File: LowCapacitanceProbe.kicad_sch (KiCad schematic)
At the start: 41 parts, among them J1 u.Fl, J2 SMA, J3 Screw_Terminal_01x01, Q1 BF998, U2 SPX3819M5-L-5-0

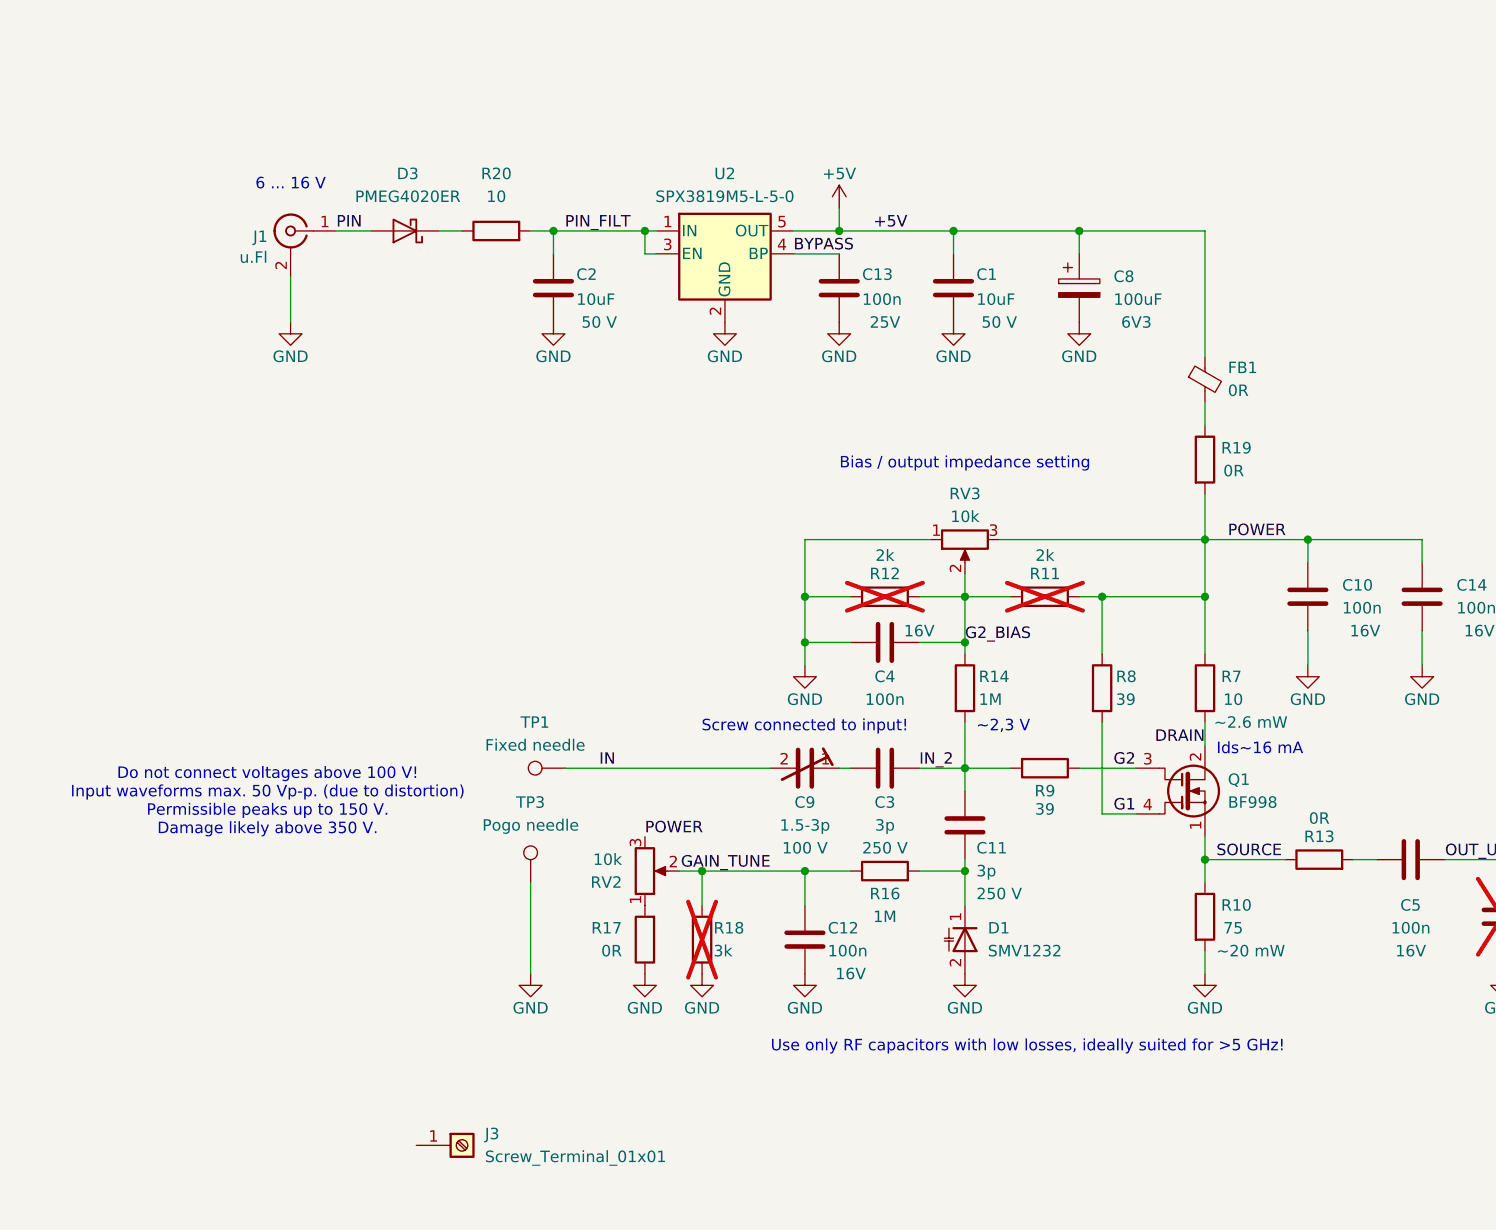
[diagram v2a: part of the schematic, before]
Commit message: Added mounting point for PCBite holder (M4 nut).
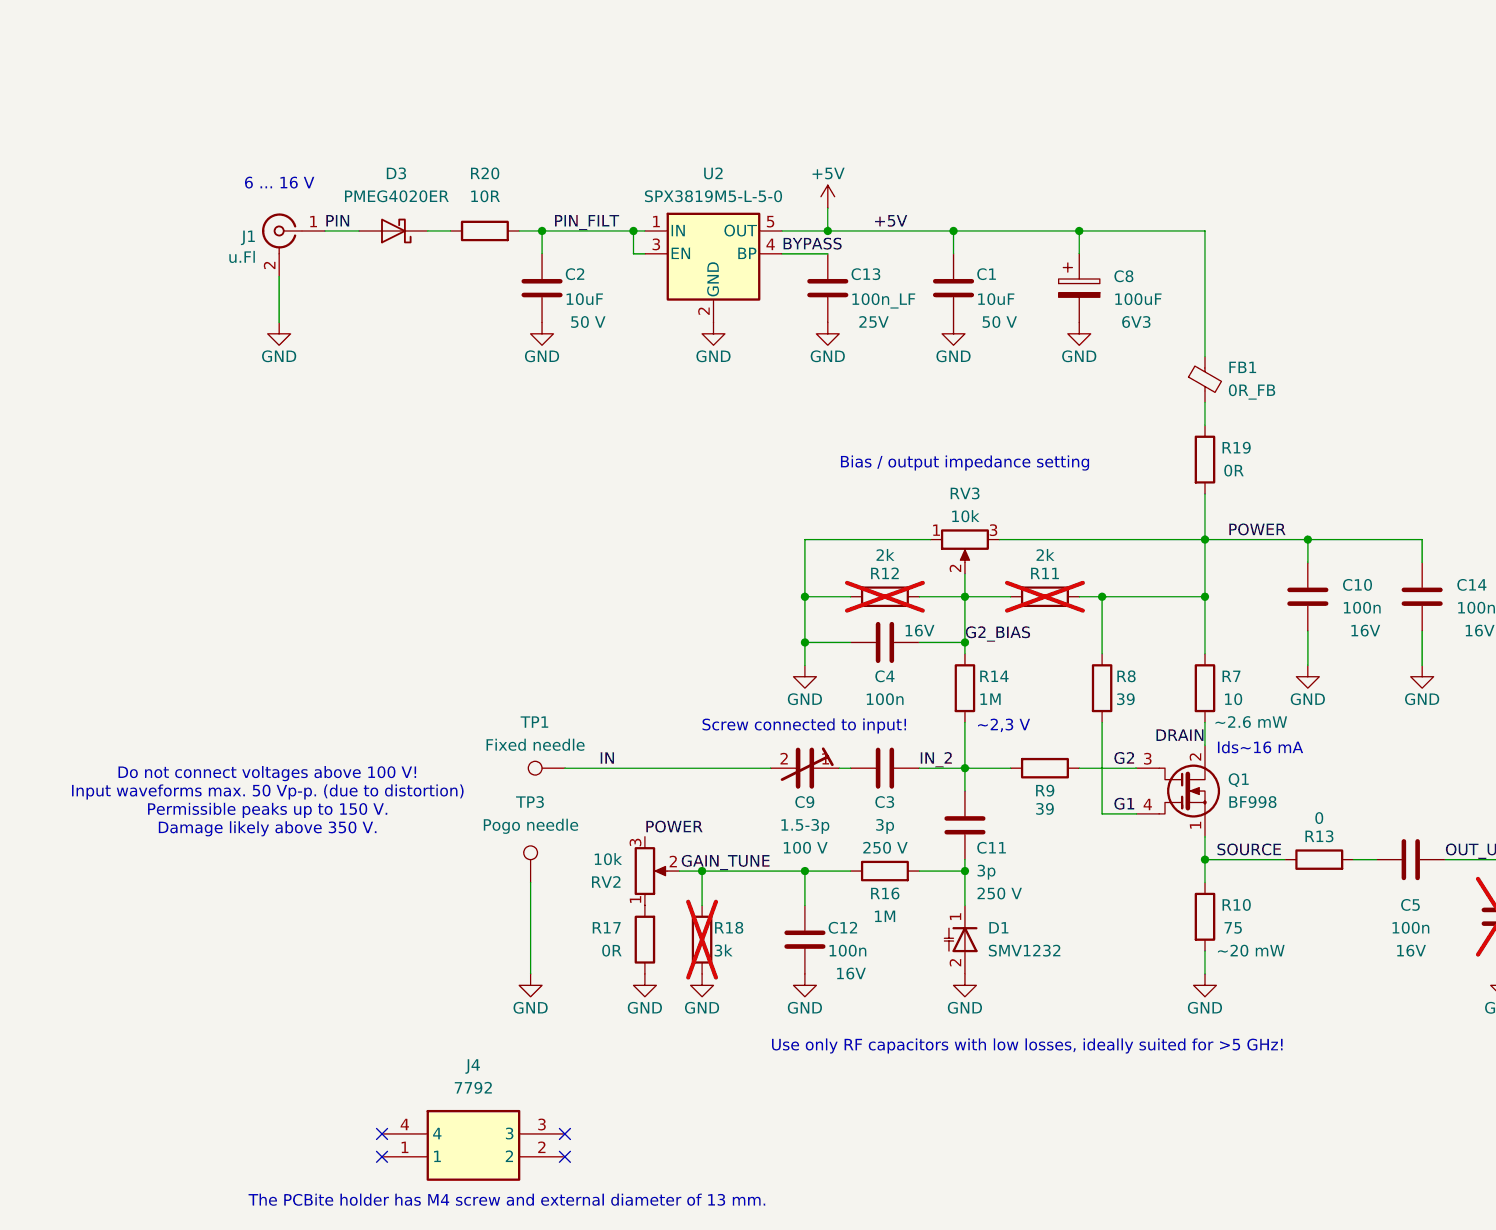
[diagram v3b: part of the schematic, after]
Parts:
- removed J3: Screw_Terminal_01x01, symbol Connector:Screw_Terminal_01x01
- added J4: 7792, 7792:7792, symbol 7792:7792
- C13: value 100n -> 100n_LF
- FB1: value 0R -> 0R_FB
- R13: value 0R -> 0
- R20: value 10 -> 10R
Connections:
- no-connect marks 0 -> 4
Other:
- note added: "The PCBite holder has M4 screw and external diameter of 13 mm."
- moved on the sheet: C13, C2, D3, J1, R20, U2

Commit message: Continued routing, modifications for better usability.
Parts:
- J4: MPN (none) -> 7792; Mouser (none) -> 534-7792
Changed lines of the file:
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@@
+			)
+		)
+		(property "MPN" "7792"
+			(at 73.66 158.75 0)
+			(effects
+				(font
+					(size 1.27 1.27)
+				)
+				(hide yes)
+			)
+		)
+		(property "Mouser" "534-7792"
+			(at 73.66 158.75 0)
+			(effects
+				(font
+					(size 1.27 1.27)
+				)
+				(hide yes)
 			)
 		)

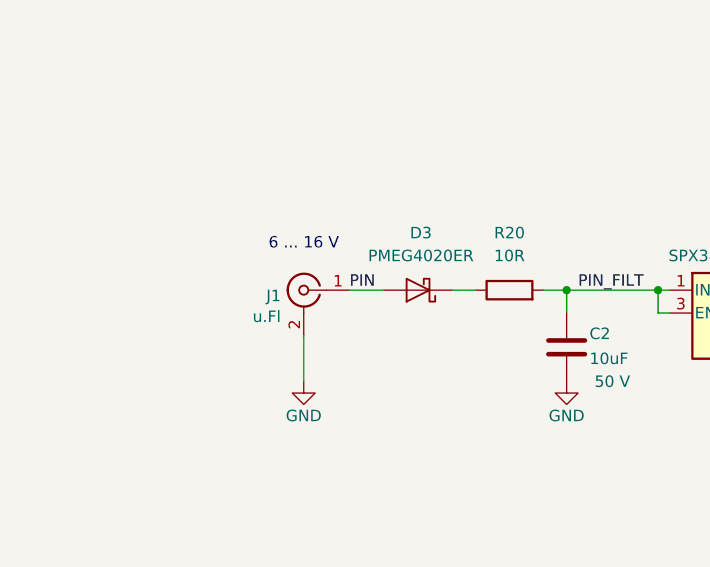
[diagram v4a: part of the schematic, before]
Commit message: Continued routing, replaced power connector.
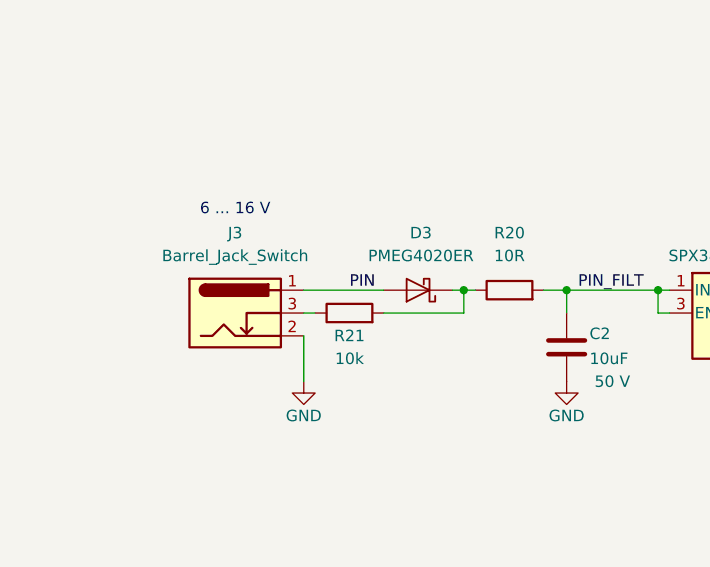
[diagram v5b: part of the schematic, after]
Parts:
- removed J1: u.Fl, Connector_Coaxial:U.FL_Molex_MCRF_73412-0110_Vertical, symbol Connector:Conn_Coaxial
- added J3: Barrel_Jack_Switch, Connector_BarrelJack:BarrelJack_Wuerth_694103107102_1.35x3.9mm, symbol Connector:Barrel_Jack_Switch
- added R21: 10k, Resistor_SMD:R_0603_1608Metric_Pad0.98x0.95mm_HandSolder, symbol Device:R
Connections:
- net GND: now also J3.2
- net PIN: now also J3.1
- net at D3.1 (K), R20.1: now also R21.2
- new net: J3.3, R21.1
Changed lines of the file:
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@@
 	(text "6 ... 16 V"
 		(exclude_from_sim no)
-		(at 62.23 53.34 0)
+		(at 54.61 49.53 0)
 		(effects
 			(font
@@
 	)
 	(junction
+		(at 80.01 58.42)
+		(diameter 0)
+		(color 0 0 0 0)
+	)
+	(junction
 		(at 120.65 99.06)
 		(diameter 0)
@@
 	(wire
 		(pts
-			(xy 78.74 58.42) (xy 81.28 58.42)
+			(xy 78.74 58.42) (xy 80.01 58.42)
 		)
 		(stroke
@@
 	(wire
 		(pts
+			(xy 62.23 60.96) (xy 63.5 60.96)
+		)
+		(stroke
+			(width 0)
+			(type default)
+		)
+	)
+	(wire
+		(pts
 			(xy 165.1 87.63) (xy 165.1 92.71)
 		)
@@
 	(wire
 		(pts
+			(xy 62.23 58.42) (xy 71.12 58.42)
+		)
+		(stroke
+			(width 0)
+			(type default)
+		)
+	)
+	(wire
+		(pts
 			(xy 120.65 92.71) (xy 120.65 99.06)
 		)
@@
 	(wire
 		(pts
+			(xy 80.01 60.96) (xy 80.01 58.42)
+		)
+		(stroke
+			(width 0)
+			(type default)
+		)
+	)
+	(wire
+		(pts
 			(xy 138.43 99.06) (xy 138.43 104.14)
 		)
@@
 	(wire
 		(pts
-			(xy 67.31 58.42) (xy 71.12 58.42)
-		)
-		(stroke
-			(width 0)
-			(type default)
-		)
-	)
-	(wire
-		(pts
 			(xy 101.6 58.42) (xy 102.87 58.42)
 		)
@@
 	(wire
 		(pts
+			(xy 80.01 58.42) (xy 81.28 58.42)
+		)
+		(stroke
+			(width 0)
+			(type default)
+		)
+	)
+	(wire
+		(pts
 			(xy 138.43 128.27) (xy 138.43 129.54)
 		)
@@
 		(pts
 			(xy 133.35 104.14) (xy 138.43 104.14)
+		)
+		(stroke
+			(width 0)
+			(type default)
+		)
+	)
+	(wire
+		(pts
+			(xy 71.12 60.96) (xy 80.01 60.96)
 		)
 		(stroke
@@
 				(path "/e63e39d7-6ac0-4ffd-8aa3-1841a4541b55"
 					(reference "R18")
+					(unit 1)
+				)
+			)
+		)
+	)
+	(symbol
+		(lib_id "Device:R")
+		(at 67.31 60.96 90)
+		(unit 1)
+		(exclude_from_sim no)
+		(in_bom yes)
+		(on_board yes)
+		(dnp no)
+		(property "Reference" "R21"
+			(at 67.31 63.5 90)
+			(effects
+				(font
+					(size 1.27 1.27)
+				)
+			)
+		)
+		(property "Value" "10k"
+			(at 67.31 66.04 90)
+			(effects
+				(font
+					(size 1.27 1.27)
+				)
+			)
+		)
+		(property "Footprint" "Resistor_SMD:R_0603_1608Metric_Pad0.98x0.95mm_HandSolder"
+			(at 67.31 62.738 90)
+			(effects
+				(font
+					(size 1.27 1.27)
+				)
+				(hide yes)
+			)
+		)
+		(property "Datasheet" "~"
+			(at 67.31 60.96 0)
+			(effects
+				(font
+					(size 1.27 1.27)
+				)
+				(hide yes)
+			)
+		)
+		(property "Description" "Resistor"
+			(at 67.31 60.96 0)
+			(effects
+				(font
+					(size 1.27 1.27)
+				)
+				(hide yes)
+			)
+		)
+		(pin "2"
+		)
+		(pin "1"
+		)
+		(instances
+			(project "LowCapacitanceProbe"
+				(path "/e63e39d7-6ac0-4ffd-8aa3-1841a4541b55"
+					(reference "R21")
+					(unit 1)
+				)
+			)
+		)
+	)
+	(symbol
+		(lib_id "Connector:Barrel_Jack_Switch")
+		(at 54.61 60.96 0)
+		(unit 1)
+		(exclude_from_sim no)
+		(in_bom yes)
+		(on_board yes)
+		(dnp no)
+		(fields_autoplaced yes)
+		(property "Reference" "J3"
+			(at 54.61 52.07 0)
+			(effects
+				(font
+					(size 1.27 1.27)
+				)
+			)
+		)
+		(property "Value" "Barrel_Jack_Switch"
+			(at 54.61 54.61 0)
+			(effects
+				(font
+					(size 1.27 1.27)
+				)
+			)
+		)
+		(property "Footprint" "Connector_BarrelJack:BarrelJack_Wuerth_694103107102_1.35x3.9mm"
+			(at 55.88 61.976 0)
+			(effects
+				(font
+					(size 1.27 1.27)
+				)
+				(hide yes)
+			)
+		)
+		(property "Datasheet" "https://www.farnell.com/datasheets/2130962.pdf"
+			(at 55.88 61.976 0)
+			(effects
+				(font
+					(size 1.27 1.27)
+				)
+				(hide yes)
+			)
+		)
+		(property "Description" "DC Barrel Jack with an internal switch"
+			(at 54.61 60.96 0)
+			(effects
+				(font
+					(size 1.27 1.27)
+				)
+				(hide yes)
+			)
+		)
+		(property "MPN" "694103107102"
+			(at 54.61 60.96 0)
+			(effects
+				(font
+					(size 1.27 1.27)
+				)
+				(hide yes)
+			)
+		)
+		(property "Mouser" "710-694103107102"
+			(at 54.61 60.96 0)
+			(effects
+				(font
+					(size 1.27 1.27)
+				)
+				(hide yes)
+			)
+		)
+		(pin "1"
+		)
+		(pin "3"
+		)
+		(pin "2"
+		)
+		(instances
+			(project ""
+				(path "/e63e39d7-6ac0-4ffd-8aa3-1841a4541b55"
+					(reference "J3")
 					(unit 1)
 				)
@@
 					(unit 1)
 				)
-			)
-		)
-	)
-	(symbol
-		(lib_id "Connector:Conn_Coaxial")
-		(at 62.23 58.42 0)
-		(mirror y)
-		(unit 1)
-		(exclude_from_sim no)
-		(in_bom yes)
-		(on_board yes)
-		(dnp no)
-		(property "Reference" "J1"
-			(at 59.69 59.055 0)
-			(effects
-				(font
-					(size 1.27 1.27)
-				)
-				(justify left)
-			)
-		)
-		(property "Value" "u.Fl"
-			(at 59.69 61.3664 0)
-			(effects
-				(font
-					(size 1.27 1.27)
-				)
-				(justify left)
-			)
-		)
-		(property "Footprint" "Connector_Coaxial:U.FL_Molex_MCRF_73412-0110_Vertical"
-			(at 62.23 58.42 0)
-			(effects
-				(font
-					(size 1.27 1.27)
-				)
-				(hide yes)
-			)
-		)
-		(property "Datasheet" "~"
-			(at 62.23 58.42 0)
-			(effects
-				(font
-					(size 1.27 1.27)
-				)
-				(hide yes)
-			)
-		)
-		(property "Description" ""
-			(at 62.23 58.42 0)
-			(effects
-				(font
-					(size 1.27 1.27)
-				)
-				(hide yes)
-			)
-		)
-		(property "MPN" "CONMHF1-SMD-G-T"
-			(at 62.23 58.42 0)
-			(effects
-				(font
-					(size 1.27 1.27)
-				)
-				(hide yes)
-			)
-		)
-		(property "LCSC Part" "C5137195"
-			(at 62.23 58.42 0)
-			(effects
-				(font
-					(size 1.27 1.27)
-				)
-				(hide yes)
-			)
-		)
-		(pin "1"
-		)
-		(pin "2"
-		)
-		(instances
-			(project "FETProbe_v2"
-				(path "/e63e39d7-6ac0-4ffd-8aa3-1841a4541b55"
-					(reference "J1")
-					(unit 1)
-				)

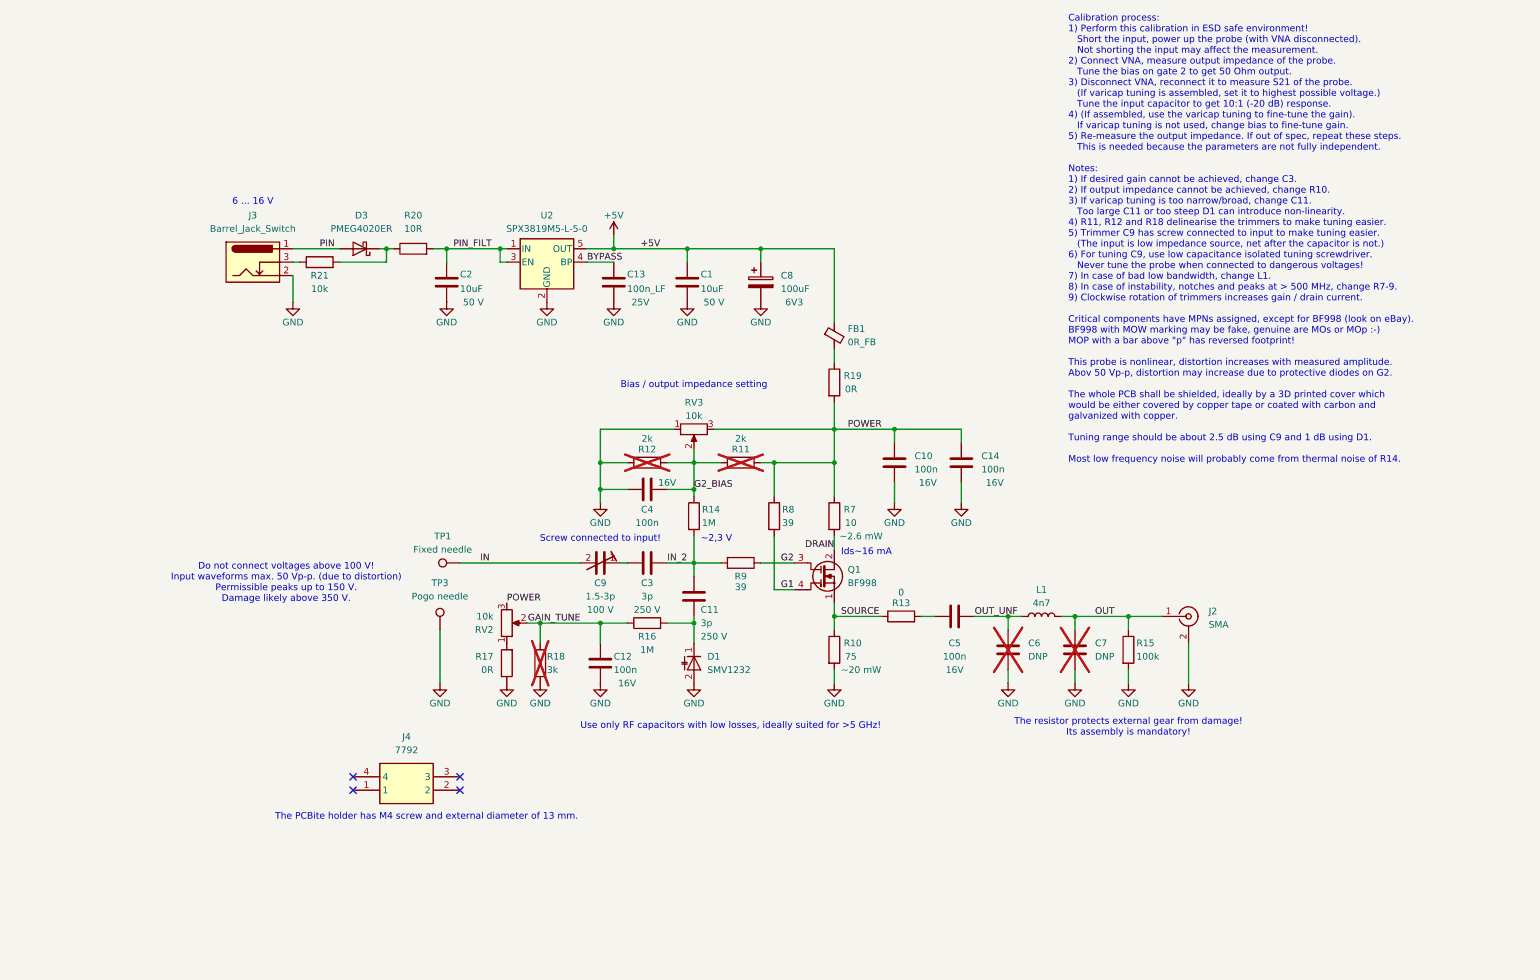
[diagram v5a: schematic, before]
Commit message: Replaced trimmers, added 3D models, continued routing and placing.
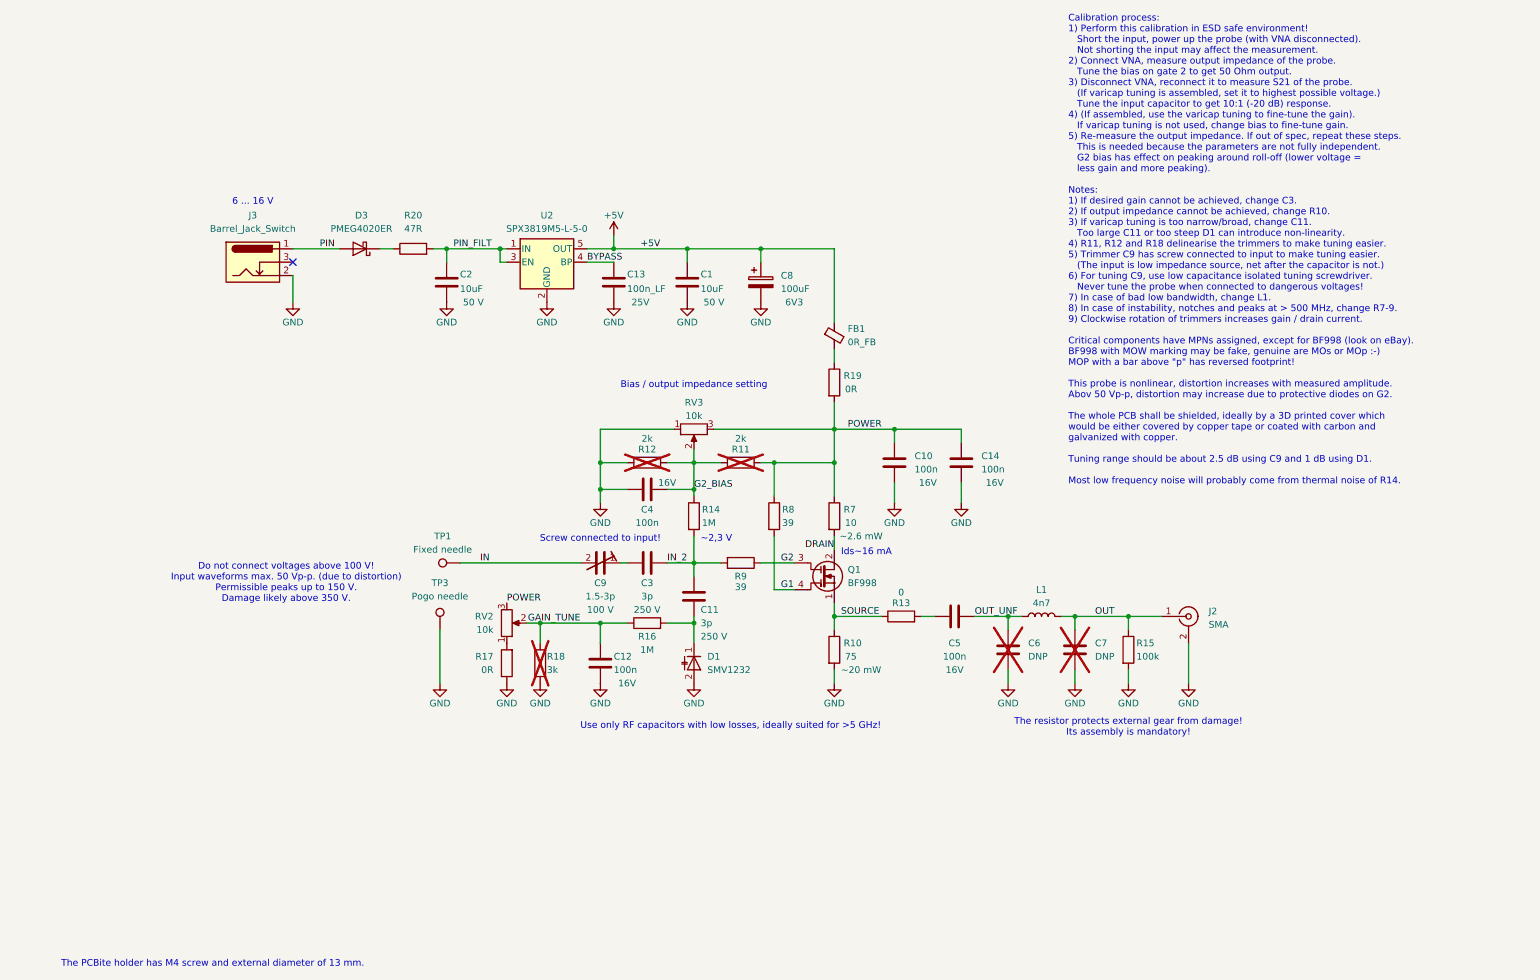
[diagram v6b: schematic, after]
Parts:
- removed J4: 7792, 7792:7792, symbol 7792:7792
- removed R21: 10k, Resistor_SMD:R_0603_1608Metric_Pad0.98x0.95mm_HandSolder, symbol Device:R
- R20: value 10R -> 47R; footprint Resistor_SMD:R_1206_3216Metric_Pad1.30x1.75mm_HandSolder -> Resistor_SMD:R_0603_1608Metric_Pad0.98x0.95mm_HandSolder
- RV2, RV3: footprint Potentiometer_SMD:Potentiometer_Bourns_3269P_Horizontal -> Potentiometer_SMD:Potentiometer_Bourns_3214J_Horizontal; MPN 3269P-1-103GLF -> 3214J-1-103E; Mouser 652-3269P-1-103GLF -> 652-3214J-1-103E
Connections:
- no-connect marks 4 -> 1
